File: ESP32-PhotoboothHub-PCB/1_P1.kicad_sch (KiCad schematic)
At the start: 28 parts, among them U10 SN74AHCT125DR, U2 ESP32-POE-ISO, U9 SN74AHCT125DR

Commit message: Fix photobooth schematic power, DMX and component footprints
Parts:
- removed ?: (no value), ProPrj_New-easyedapro:, symbol ProPrj_New-easyedapro:Drawing-Symbol_A4
- added C19, C20: 1uF / 50V, Capacitor_SMD:C_0603_1608Metric, symbol PowerFixes:C
- added JP1: EXT_5V_ENABLE, Connector_PinHeader_2.54mm:PinHeader_1x02_P2.54mm_Vertical, symbol PowerFixes:EXT_5V_ENABLE
- added U12: MAX40200AUK+T, Package_TO_SOT_SMD:SOT-23-5, symbol PowerFixes:MAX40200AUK
- C14, C15, C16, C7: value 470uF -> 470uF / 16V; footprint ProPrj_New-easyedapro:CAP-SMD_BD6.3-L6.6-W6.6-LS7.6-RD -> Capacitor_SMD:CP_Elec_8x10.5; Assembly Class (none) -> JLCPCB Extended (checked 2026-09-08); standard catalog part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; LCSC Part Name 470uF ±20% 25V -> 470uF 16V aluminum electrolytic SMD 8x10.2mm; Manufacturer HRK(鸿瑞凯电子) -> Honor Elec; Manufacturer Part 25V470uF CD110 -> RVT1C471M0810; Supplier Part C2960234 -> C3341; Tolerance (none) -> 20%; Voltage Rating (none) -> 16 V
- C8, C9: footprint ProPrj_New-easyedapro:C0603 -> Capacitor_SMD:C_0603_1608Metric
- D1: renamed from PWR_LED; value NCD0805R1 -> Power; footprint ProPrj_New-easyedapro:LED0805-R-RD -> Photobooth:LED_0805_2012Metric_A1K2; Function (none) -> Power indicator; Model (none) -> NCD0805R1; Previous Reference (none) -> PWR_LED
- F1: renamed from FUSE_PSU; value PTF-77 -> TBD A; footprint ProPrj_New-easyedapro:FUSE-TH_L24.4-W9.4-P22.60 -> Photobooth:Fuseholder_OptiFuse_CNT-06_MICRO2; Assembly (none) -> Fit holder and separately selected fuse; verify seating, ex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; Fitted Fuse (none) -> OptiFuse ANT/APT; current rating TBD before manufacture; Function (none) -> Main supply; LCSC Part Name 保险丝座 5x20mm 绿色 2件套 -> (none); Manufacturer XFCN(兴飞) -> OptiFuse; Manufacturer Part PTF-77 -> CNT-06; Model (none) -> CNT-06 / MICRO2; Previous Reference (none) -> FUSE_PSU; Supplier LCSC -> OptiFuse; Supplier Part C717030 -> CNT-06
- F2: renamed from FUSE_LIGHT_FRONT; value PTF-77 -> TBD A; footprint ProPrj_New-easyedapro:FUSE-TH_L24.4-W9.4-P22.60 -> Photobooth:Fuseholder_OptiFuse_CNT-06_MICRO2; Assembly (none) -> Fit holder and separately selected fuse; verify seating, ex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; Fitted Fuse (none) -> OptiFuse ANT/APT; current rating TBD before manufacture; Function (none) -> Front lighting; LCSC Part Name 保险丝座 5x20mm 绿色 2件套 -> (none); Manufacturer XFCN(兴飞) -> OptiFuse; Manufacturer Part PTF-77 -> CNT-06; Model (none) -> CNT-06 / MICRO2; Previous Reference (none) -> FUSE_LIGHT_FRONT; Supplier LCSC -> OptiFuse; Supplier Part C717030 -> CNT-06
- F3: renamed from FUSE_LIGHT_PRINTER; value PTF-77 -> TBD A; footprint ProPrj_New-easyedapro:FUSE-TH_L24.4-W9.4-P22.60 -> Photobooth:Fuseholder_OptiFuse_CNT-06_MICRO2; Assembly (none) -> Fit holder and separately selected fuse; verify seating, ex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; Fitted Fuse (none) -> OptiFuse ANT/APT; current rating TBD before manufacture; Function (none) -> Printer lighting; LCSC Part Name 保险丝座 5x20mm 绿色 2件套 -> (none); Manufacturer XFCN(兴飞) -> OptiFuse; Manufacturer Part PTF-77 -> CNT-06; Model (none) -> CNT-06 / MICRO2; Previous Reference (none) -> FUSE_LIGHT_PRINTER; Supplier LCSC -> OptiFuse; Supplier Part C717030 -> CNT-06
- F4: renamed from FUSE_LIGHT_TRUSS; value PTF-77 -> TBD A; footprint ProPrj_New-easyedapro:FUSE-TH_L24.4-W9.4-P22.60 -> Photobooth:Fuseholder_OptiFuse_CNT-06_MICRO2; Assembly (none) -> Fit holder and separately selected fuse; verify seating, ex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; Fitted Fuse (none) -> OptiFuse ANT/APT; current rating TBD before manufacture; Function (none) -> Down lighting; LCSC Part Name 保险丝座 5x20mm 绿色 2件套 -> (none); Manufacturer XFCN(兴飞) -> OptiFuse; Manufacturer Part PTF-77 -> CNT-06; Model (none) -> CNT-06 / MICRO2; Previous Reference (none) -> FUSE_LIGHT_TRUSS; Supplier LCSC -> OptiFuse; Supplier Part C717030 -> CNT-06
- J1: renamed from CON_PSU; value WJ142R-5.08-02P-14-00A -> 5 V supply; footprint ProPrj_New-easyedapro:CONN-TH_KF250NH-3.5-2P -> Photobooth:PhoenixContact_SPT_1.5_2-V-3.5_1990850; Function (none) -> 5 V supply; LCSC Part Name 5.08mm 每排P数:2 排数:1 -> (none); Manufacturer KANGNEX(康奈克斯电气) -> Phoenix Contact; Manufacturer Part WJ142R-5.08-02P-14-00A -> 1990850; Model (none) -> SPT 1,5/2-V-3,5; Previous Reference (none) -> CON_PSU; Supplier LCSC -> Phoenix Contact; Supplier Part C35616 -> 1990850
- J2: renamed from CON_CMD_BTN; value WJ142R-5.08-02P-14-00A -> Command button; footprint ProPrj_New-easyedapro:CONN-TH_KF250NH-3.5-2P -> Photobooth:PhoenixContact_SPT_1.5_2-V-3.5_1990850; Function (none) -> Command button; LCSC Part Name 5.08mm 每排P数:2 排数:1 -> (none); Manufacturer KANGNEX(康奈克斯电气) -> Phoenix Contact; Manufacturer Part WJ142R-5.08-02P-14-00A -> 1990850; Model (none) -> SPT 1,5/2-V-3,5; Previous Reference (none) -> CON_CMD_BTN; Supplier LCSC -> Phoenix Contact; Supplier Part C35616 -> 1990850
- J3: renamed from CON_LIGHT_FRONT; value WJ142R-5.08-04P-14-00A -> Front lighting; footprint ProPrj_New-easyedapro:CONN-TH_KF250NH-3.5-4P -> Photobooth:PhoenixContact_SPT_1.5_4-V-3.5_1990876; Function (none) -> Front lighting; LCSC Part Name 5.08mm 每排P数:4 排数:1 -> (none); Manufacturer KANGNEX(康奈克斯电气) -> Phoenix Contact; Manufacturer Part WJ142R-5.08-04P-14-00A -> 1990876; Model (none) -> SPT 1,5/4-V-3,5; Previous Reference (none) -> CON_LIGHT_FRONT; Supplier LCSC -> Phoenix Contact; Supplier Part C80055 -> 1990876
- J4: renamed from CON_LIGHT_PRINTER; value WJ142R-5.08-04P-14-00A -> Printer lighting; footprint ProPrj_New-easyedapro:CONN-TH_KF250NH-3.5-4P -> Photobooth:PhoenixContact_SPT_1.5_4-V-3.5_1990876; Function (none) -> Printer lighting; LCSC Part Name 5.08mm 每排P数:4 排数:1 -> (none); Manufacturer KANGNEX(康奈克斯电气) -> Phoenix Contact; Manufacturer Part WJ142R-5.08-04P-14-00A -> 1990876; Model (none) -> SPT 1,5/4-V-3,5; Previous Reference (none) -> CON_LIGHT_PRINTER; Supplier LCSC -> Phoenix Contact; Supplier Part C80055 -> 1990876
- J5: renamed from CON_LIGHT_DOWN; value WJ142R-5.08-04P-14-00A -> Down lighting; footprint ProPrj_New-easyedapro:CONN-TH_KF250NH-3.5-4P -> Photobooth:PhoenixContact_SPT_1.5_4-V-3.5_1990876; Function (none) -> Down lighting; LCSC Part Name 5.08mm 每排P数:4 排数:1 -> (none); Manufacturer KANGNEX(康奈克斯电气) -> Phoenix Contact; Manufacturer Part WJ142R-5.08-04P-14-00A -> 1990876; Model (none) -> SPT 1,5/4-V-3,5; Previous Reference (none) -> CON_LIGHT_DOWN; Supplier LCSC -> Phoenix Contact; Supplier Part C80055 -> 1990876
- R16, R17, R18, R19, R20, R21, R22, R27: footprint ProPrj_New-easyedapro:R0603 -> Resistor_SMD:R_0603_1608Metric
- U10, U9: footprint ProPrj_New-easyedapro:SOIC-14_L8.7-W3.9-P1.27-LS6.0-BL -> Package_SO:SOIC-14_3.9x8.7mm_P1.27mm
- U2: footprint ProPrj_New-easyedapro:COMM-TH_20P-P2.54_ESP32-POE-ISO -> Photobooth:Olimex_ESP32-POE-ISO
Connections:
- net +5V: now also C19.1, U12.1 (VDD), U12.3 (EN); no longer U2.1 (+5V)
- net GND: now also C19.2, C20.2, U12.2 (GND)
- new net: C20.1, JP1.1 (A), U12.5 (OUT)
- new net MCU_5V: JP1.2 (B), U2.1 (+5V)
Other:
- note added: "Controller supply isolation"
- note added: "External supply: regulated 4.75-5.25 V. Place C19/C20 at U12. Lighting current bypasses U12."
- note added: "GPIO0 reserved for boot and Ethernet."
- note added: "JP1: fit shunt for external 5 V; REMOVE before powered USB or for PoE-only operation."
- note removed: "Neccessary for boot and ethernet. Do not use"
- title: (none) -> Photobooth Hub - Controller and lighting
- moved on the sheet: C14, C15, C16, C7, C8, C9, D1, F1, F2, F3, F4, J1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

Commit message: Add PCB placement with Ethernet on the right
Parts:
- JP1: Manufacturer (none) -> Harwin; Manufacturer Part (none) -> M20-9990246; Mating Shunt (none) -> Harwin M7566-46; remove before powered USB
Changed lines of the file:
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@@
 (property "Value" "EXT_5V_ENABLE" (at 245.24 140.97 0) (effects (font (size 1.27 1.27))))
 (property "Footprint" "Connector_PinHeader_2.54mm:PinHeader_1x02_P2.54mm_Vertical" (at 238.76 146.05 0) (hide yes) (effects (font (size 1.27 1.27))))
-(property "Datasheet" "" (at 238.76 146.05 0) (hide yes) (effects (font (size 1.27 1.27))))
+(property "Datasheet" "https://www.harwin.com/products/M20-9990246" (at 238.76 146.05 0) (hide yes) (effects (font (size 1.27 1.27))))
 (property "Description" "Two-pin header with removable shunt. Fit for external 5 V; remove before powered USB or for PoE-only operation." (at 238.76 146.05 0) (hide yes) (effects (font (size 1.27 1.27))))
 (property "Assembly Note" "Populate the 1x02 2.54 mm header and supply a removable shunt. Fit shunt for external 5 V. Remove before powered USB or for PoE-only operation." (at 238.76 146.05 0) (hide yes) (effects (font (size 1.27 1.27))))
+    (property "Manufacturer" "Harwin" (at 238.76 146.05 0)
+      (effects (font (size 1.27 1.27)) (hide yes))
+    )
+    (property "Manufacturer Part" "M20-9990246" (at 238.76 146.05 0)
+      (effects (font (size 1.27 1.27)) (hide yes))
+    )
+    (property "Mating Shunt" "Harwin M7566-46; remove before powered USB" (at 238.76 146.05 0)
+      (effects (font (size 1.27 1.27)) (hide yes))
+    )
 (pin "1")
 (pin "2")

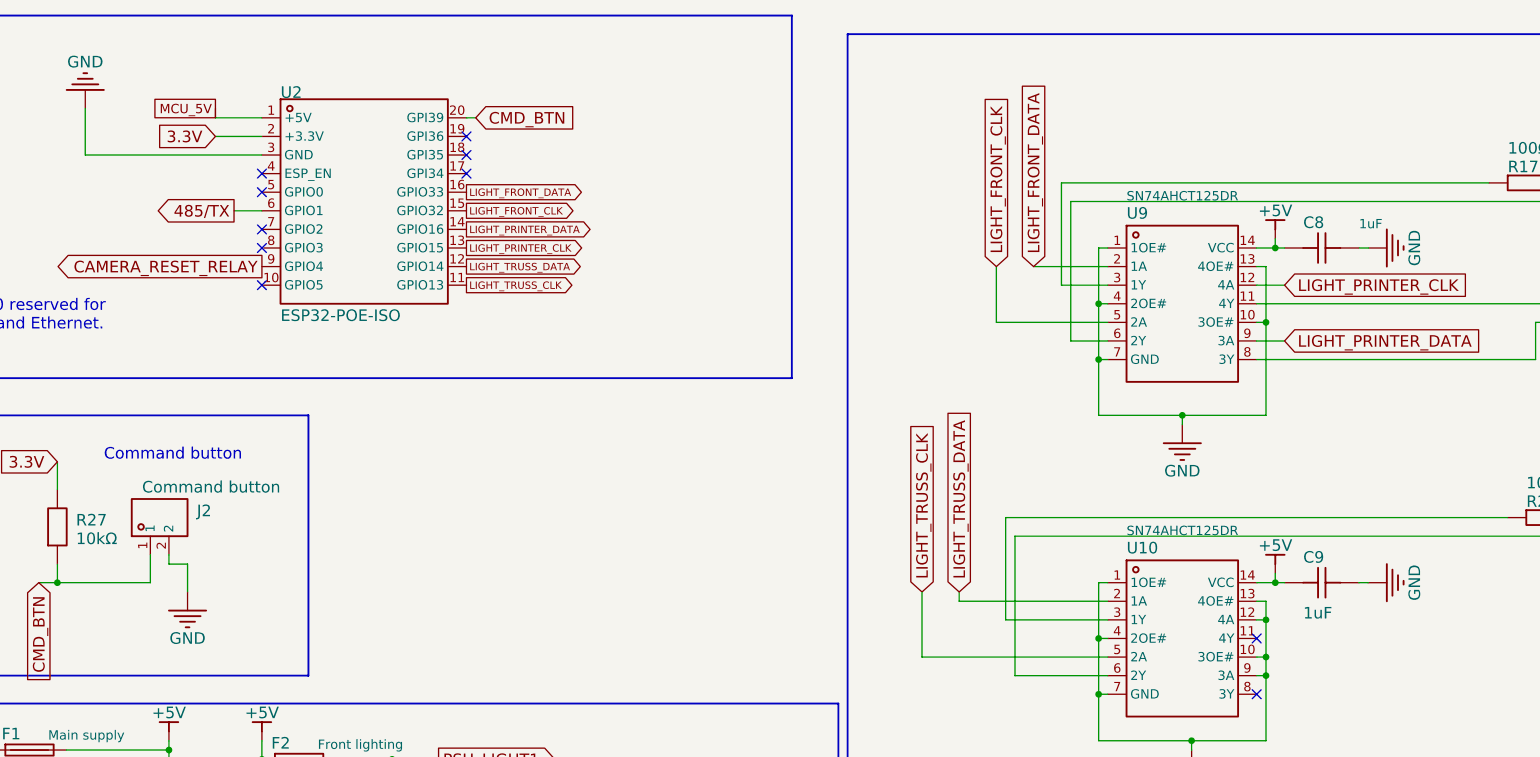
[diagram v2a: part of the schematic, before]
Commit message: Complete PCB routing with protected power bus and verified isolation
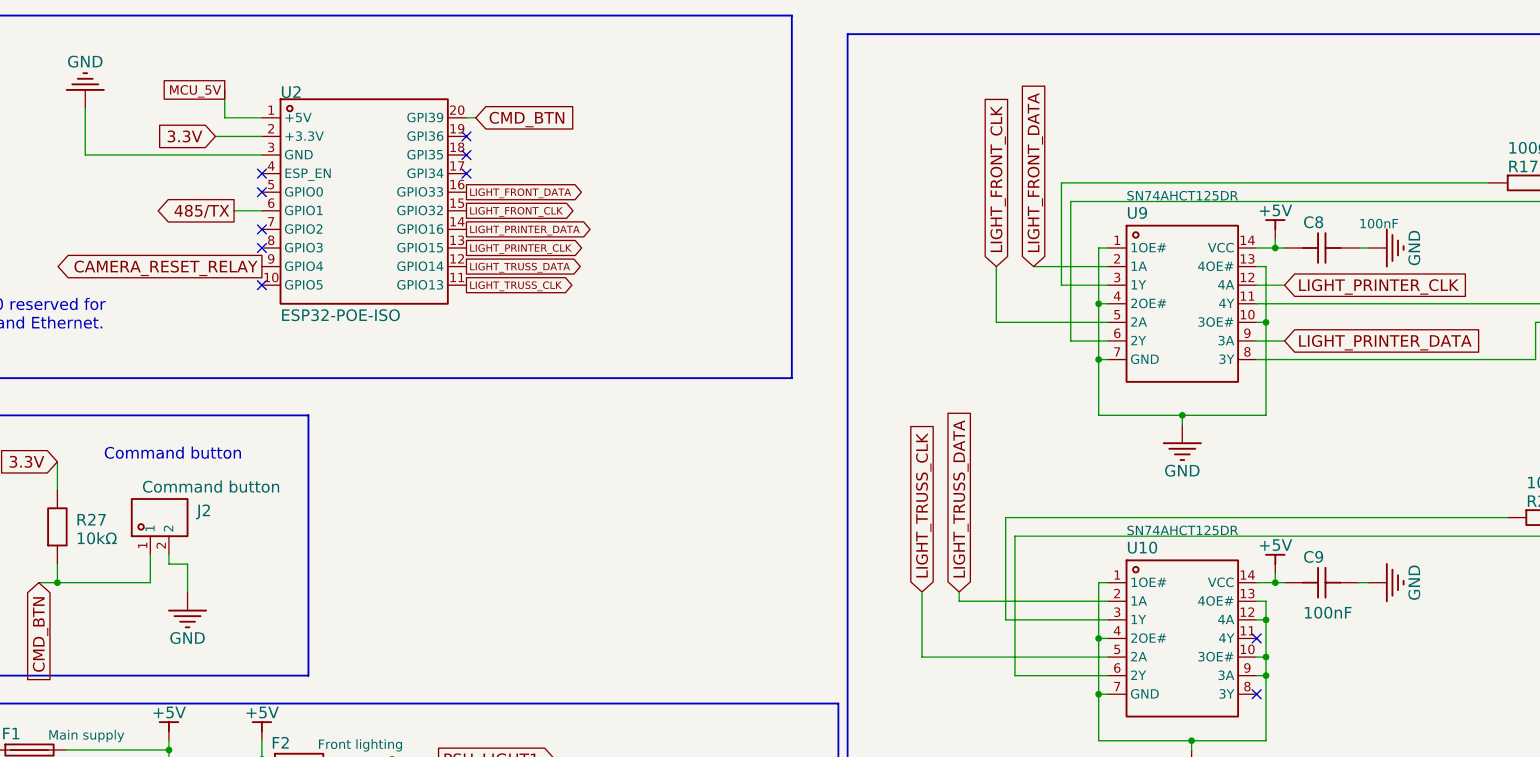
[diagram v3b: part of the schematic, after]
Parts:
- C8, C9: value 1uF -> 100nF; LCSC Part Name 1uF ±10% 50V -> 100nF ±10% 50V; Manufacturer SAMSUNG(三星) -> YAGEO(国巨); Manufacturer Part CL10A105KB8NNNC -> CC0603KRX7R9BB104; Supplier Part C15849 -> C14663
